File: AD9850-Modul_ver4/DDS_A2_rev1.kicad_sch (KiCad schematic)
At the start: 69 parts, among them J1 Conn_01x02_Male, J2 Conn_01x16_Male, J3 Conn_01x20_Male, J4 Conn_01x20_Male, J5 AVR-ISP-6, J6 Conn_01x03_Male, J7 Conn_02x05_Odd_Even, Q1 BC547, Q2 BC556, Q3 BD139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

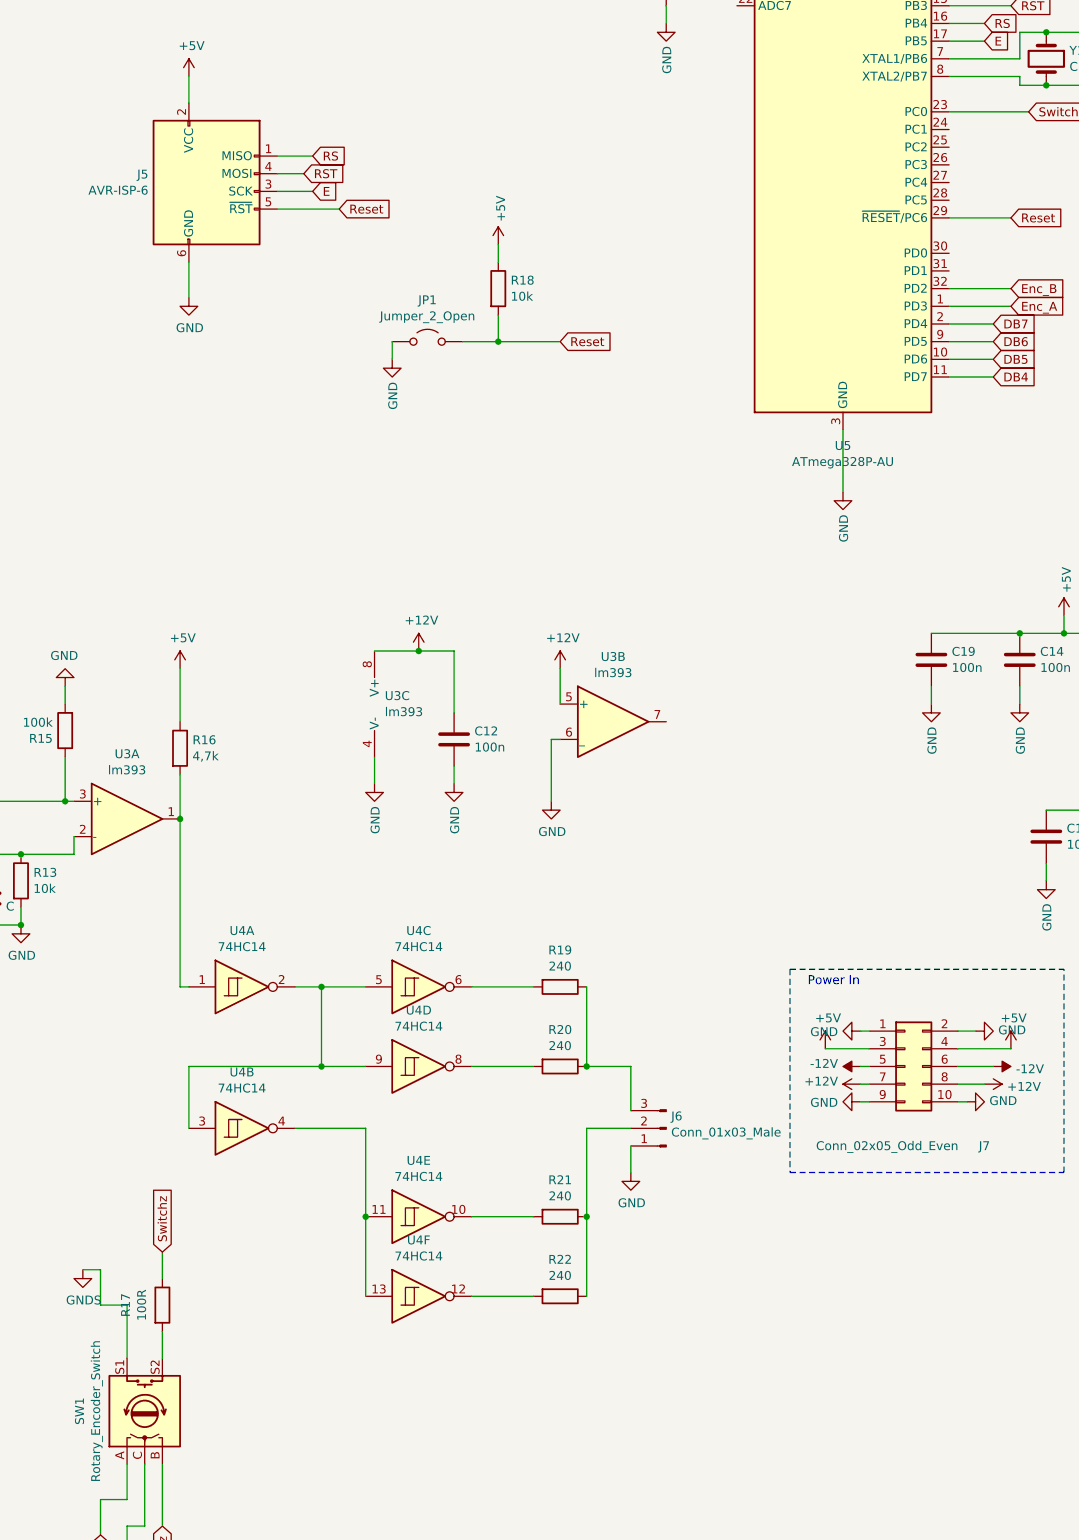
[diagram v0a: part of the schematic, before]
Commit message: Useless Adder auf V2.0 gebracht. Software finalisiert, Platine benötigt noch Arbeit
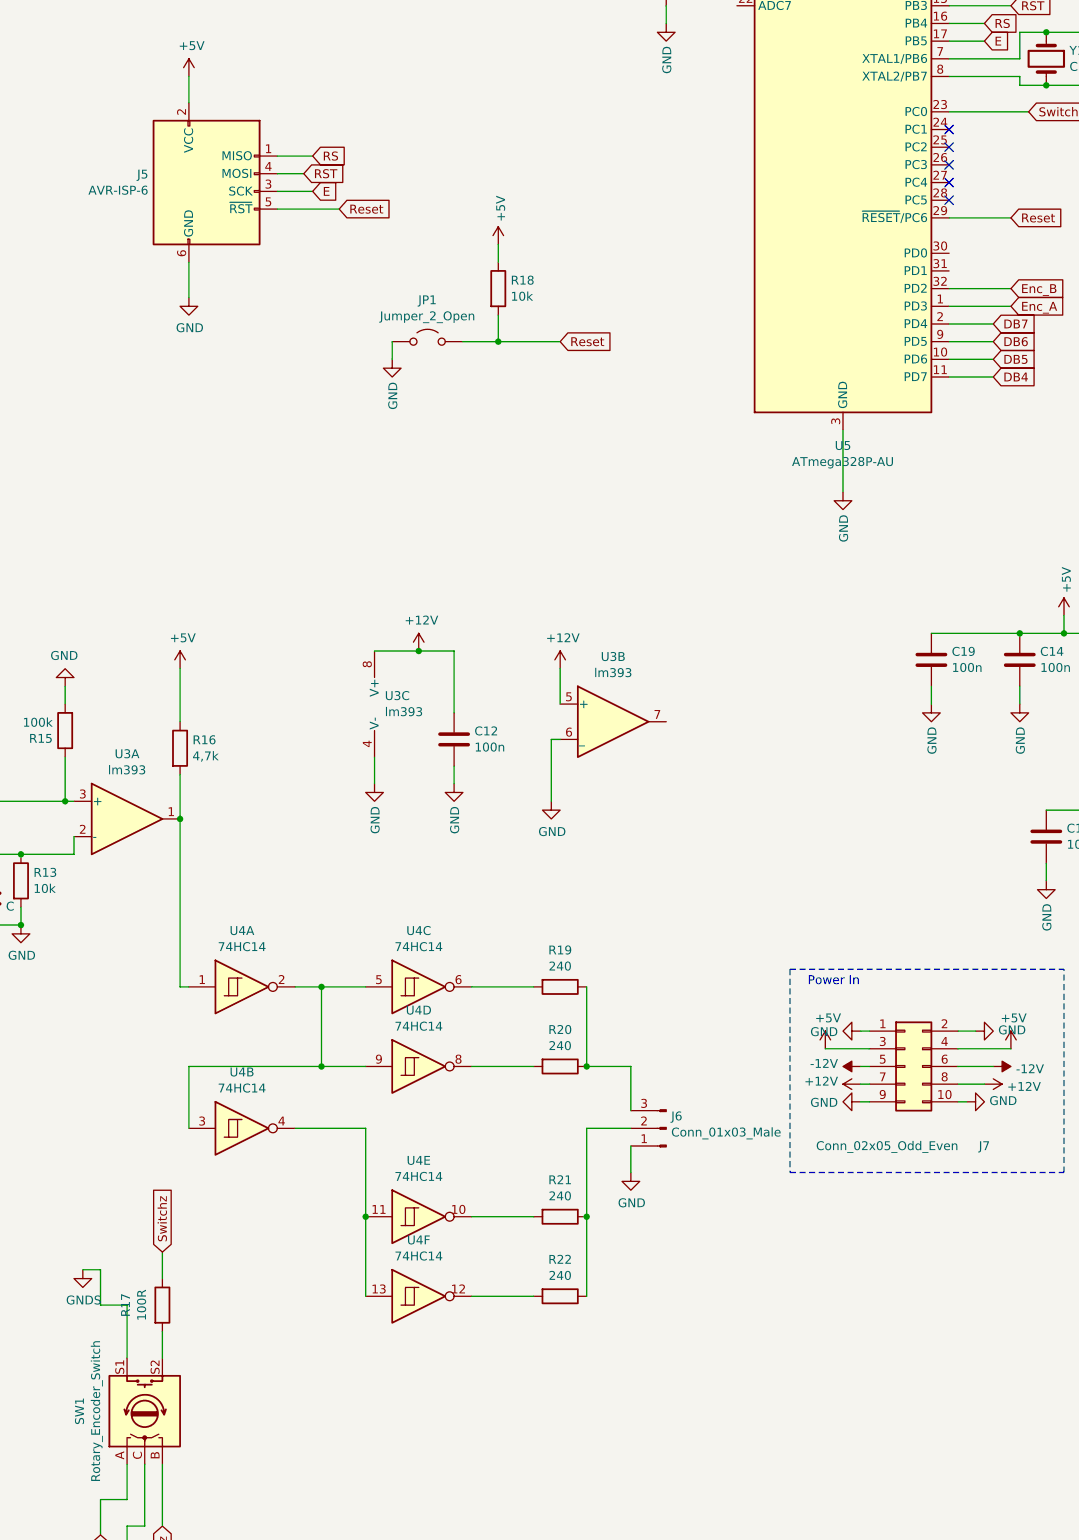
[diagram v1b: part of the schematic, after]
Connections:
- no-connect marks 12 -> 17
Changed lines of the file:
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@@
 (kicad_sch
-	(version 20231120)
+	(version 20250114)
 	(generator "eeschema")
-	(generator_version "8.0")
+	(generator_version "9.0")
 	(paper "A3")
 	(title_block
@@
 		(comment 2 "Basierend auf Schaltung DDS VFO  Richard Visokey AD7C www.ad7c.com")
 	)
+	(text "Pinheader Zusatzplatine"
+		(exclude_from_sim no)
+		(at 92.71 214.63 0)
+		(effects
+			(font
+				(size 1.27 1.27)
+			)
+			(justify left bottom)
+		)
+	)
+	(text "Verstärkung 3"
+		(exclude_from_sim no)
+		(at 107.95 149.86 0)
+		(effects
+			(font
+				(size 1.27 1.27)
+			)
+			(justify left bottom)
+		)
+	)
+	(text "Verstärker"
+		(exclude_from_sim no)
+		(at 24.13 71.12 0)
+		(effects
+			(font
+				(size 1.27 1.27)
+			)
+			(justify left bottom)
+		)
+	)
+	(text "Pinheader Hauptplatine"
+		(exclude_from_sim no)
+		(at 77.47 199.39 0)
+		(effects
+			(font
+				(size 1.27 1.27)
+			)
+			(justify left bottom)
+		)
+	)
+	(text "DDS Modul\n"
+		(exclude_from_sim no)
+		(at 124.46 17.78 0)
+		(effects
+			(font
+				(size 1.27 1.27)
+			)
+			(justify left bottom)
+		)
+	)
+	(text "Verstärkung 10"
+		(exclude_from_sim no)
+		(at 52.07 146.05 0)
+		(effects
+			(font
+				(size 1.27 1.27)
+			)
+			(justify left bottom)
+		)
+	)
+	(text "Power In"
+		(exclude_from_sim no)
+		(at 344.17 194.31 0)
+		(effects
+			(font
+				(size 1.27 1.27)
+			)
+			(justify left bottom)
+		)
+	)
+	(text "Display HD1602 Pinheader"
+		(exclude_from_sim no)
+		(at 46.99 240.03 0)
+		(effects
+			(font
+				(size 1.27 1.27)
+			)
+			(justify left bottom)
+		)
+	)
 	(junction
 		(at 163.83 102.87)
@@
 	)
 	(no_connect
+		(at 364.49 81.28)
+	)
+	(no_connect
 		(at 165.1 44.45)
 	)
@@
 	)
 	(no_connect
+		(at 364.49 76.2)
+	)
+	(no_connect
 		(at 165.1 40.64)
 	)
 	(no_connect
+		(at 364.49 73.66)
+	)
+	(no_connect
+		(at 364.49 71.12)
+	)
+	(no_connect
+		(at 364.49 78.74)
+	)
+	(no_connect
 		(at 250.19 -35.56)
 	)
@@
 		)
 	)
-	(text "Pinheader Zusatzplatine"
-		(exclude_from_sim no)
-		(at 92.71 214.63 0)
-		(effects
-			(font
-				(size 1.27 1.27)
-			)
-			(justify left bottom)
-		)
-	)
-	(text "Verstärkung 3"
-		(exclude_from_sim no)
-		(at 107.95 149.86 0)
-		(effects
-			(font
-				(size 1.27 1.27)
-			)
-			(justify left bottom)
-		)
-	)
-	(text "Verstärker"
-		(exclude_from_sim no)
-		(at 24.13 71.12 0)
-		(effects
-			(font
-				(size 1.27 1.27)
-			)
-			(justify left bottom)
-		)
-	)
-	(text "Pinheader Hauptplatine"
-		(exclude_from_sim no)
-		(at 77.47 199.39 0)
-		(effects
-			(font
-				(size 1.27 1.27)
-			)
-			(justify left bottom)
-		)
-	)
-	(text "DDS Modul\n"
-		(exclude_from_sim no)
-		(at 124.46 17.78 0)
-		(effects
-			(font
-				(size 1.27 1.27)
-			)
-			(justify left bottom)
-		)
-	)
-	(text "Verstärkung 10"
-		(exclude_from_sim no)
-		(at 52.07 146.05 0)
-		(effects
-			(font
-				(size 1.27 1.27)
-			)
-			(justify left bottom)
-		)
-	)
-	(text "Power In"
-		(exclude_from_sim no)
-		(at 344.17 194.31 0)
-		(effects
-			(font
-				(size 1.27 1.27)
-			)
-			(justify left bottom)
-		)
-	)
-	(text "Display HD1602 Pinheader"
-		(exclude_from_sim no)
-		(at 46.99 240.03 0)
-		(effects
-			(font
-				(size 1.27 1.27)
-			)
-			(justify left bottom)
-		)
-	)
 	(global_label "DB7z"
 		(shape input)
@@
 		)
 	)
+	(embedded_fonts no)
 )
